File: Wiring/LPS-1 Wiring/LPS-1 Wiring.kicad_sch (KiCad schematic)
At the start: 25 parts, among them J1 Block_Connector_01_b, J10 Block_Connector_01_b, J101 Block_Connector_01_b, J102 Block_Connector_01_b, J11 Block_Connector_01_b, J12 Block_Connector_01_b, J2 Block_Connector_01_b, J3 Block_Connector_01_b, J4 Block_Connector_01_b, J5 Block_Connector_01_b, J500 GND Block, J6 Block_Connector_01_b, J7 Pwr Block, J8 Block_Connector_01_b, J9 Block_Connector_01_b, SW2 TRU Components NO

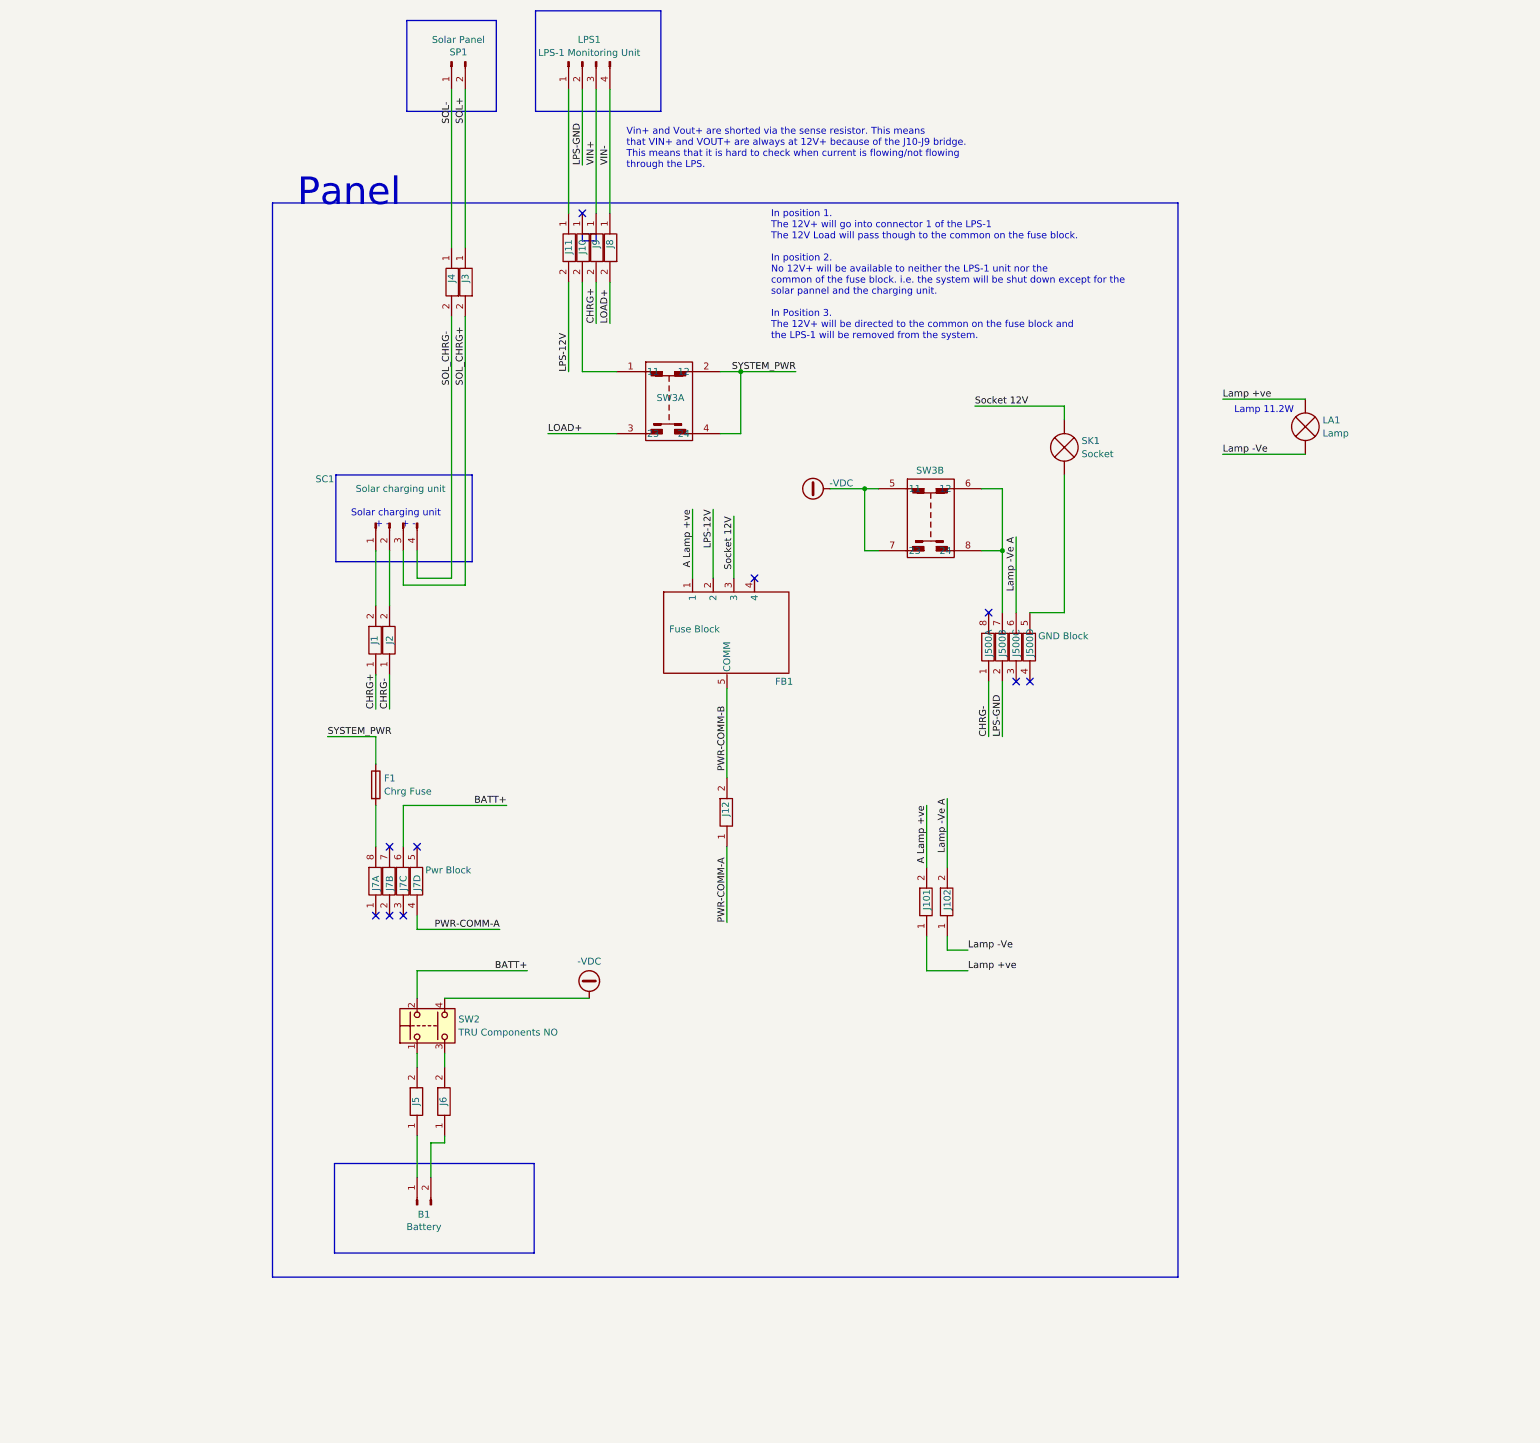
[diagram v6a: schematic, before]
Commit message: Reconfigured the LPS-1 wiring
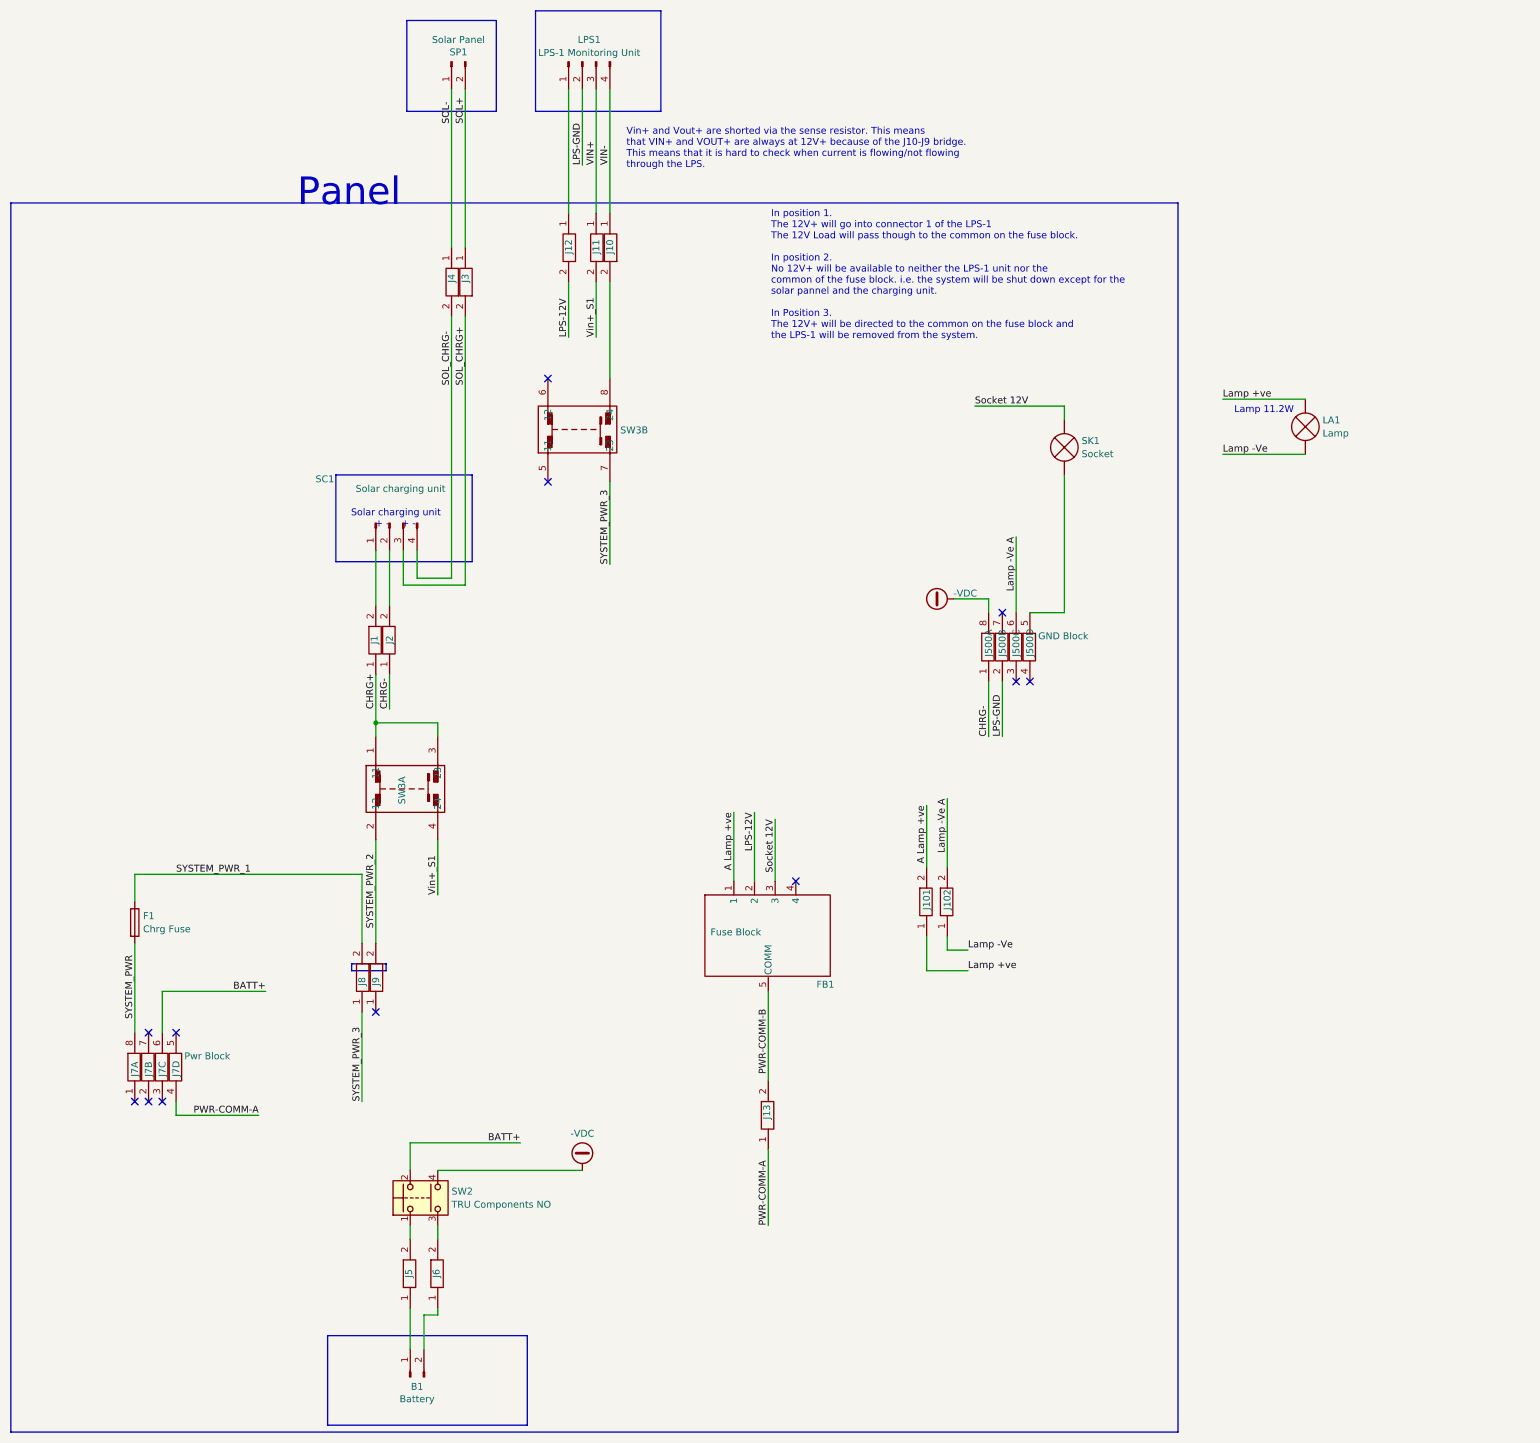
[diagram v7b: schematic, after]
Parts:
- removed J10: Block_Connector_01_b, Wiring:Degson_01_PC2.5-01P-11-00AH-1_5.2, symbol Wiring:Block_Connector_01_Pin
- added J8, J9: Block_Connector_01_b, Wiring:Degson_01_PC2.5-01P-11-00AH-1_5.2, symbol Wiring:Block_Connector_01_Pin
- renumbered J8 to J10, J9 to J11, J11 to J12, J12 to J13
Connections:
- net -VDC: now also J500.8; no longer SW3.5 (11), SW3.7 (23)
- net CHRG+: now also SW3.1 (11), SW3.3 (23); no longer J11.2
- net SYSTEM_PWR: now also F1.2, J7.8; no longer F1.1, SW3.2 (12), SW3.4 (24)
- net LOAD+: no longer names the net of J10.2
- net LOAD+: now also SW3.8 (24); no longer SW3.3 (23)
- new net SYSTEM_PWR_1: F1.1, J8.2
- new net SYSTEM_PWR_2: J9.2, SW3.2 (12)
- new net SYSTEM_PWR_3: J8.1, SW3.7 (23)
- new net Vin+_S1: J11.2, SW3.4 (24)
- now unconnected: J500.7, SW3.6 (12)
- no-connect marks 10 -> 12
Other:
- moved on the sheet: B1, F1, FB1, J13, J5, J6, J7A, J7B, J7C, J7D, SW2, SW3A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

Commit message: Panel wiring update
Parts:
- added J13: Block_Connector_01_b, Wiring:Degson_01_PC2.5-01P-11-00AH-1_5.2, symbol Wiring:Block_Connector_01_Pin
- renumbered J13 to J14
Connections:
- net LPS-12V: now also J12.1, LPS1.1 (Pin_1); no longer FB1.2, J12.2
- net LPS-12V_2: now reaches SW3.5 (11)
- net LPS-12V_2: now also J13.2
- net LPS-12V_3: now reaches SW3.6 (12)
- net LPS-12V_3: now also J12.2
- net VIN+ renamed Vin+
- net VIN- renamed Vout+
- new net LPS-12V_1: FB1.2, J13.1
- no-connect marks 12 -> 10
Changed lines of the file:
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@@
 	)
 	(no_connect
-		(at 146.05 83.82)
-	)
-	(no_connect
-		(at 146.05 102.87)
-	)
-	(no_connect
 		(at 74.93 217.17)
 	)
@@
 	(wire
 		(pts
+			(xy 149.86 76.2) (xy 146.05 76.2)
+		)
+		(stroke
+			(width 0)
+			(type default)
+		)
+	)
+	(wire
+		(pts
+			(xy 146.05 76.2) (xy 146.05 83.82)
+		)
+		(stroke
+			(width 0)
+			(type default)
+		)
+	)
+	(wire
+		(pts
 			(xy 125.73 229.87) (xy 152.4 229.87)
 		)
@@
 	(wire
 		(pts
+			(xy 146.05 125.73) (xy 146.05 135.89)
+		)
+		(stroke
+			(width 0)
+			(type default)
+		)
+	)
+	(wire
+		(pts
 			(xy 77.47 219.71) (xy 92.71 219.71)
 		)
@@
 	(wire
 		(pts
+			(xy 146.05 102.87) (xy 146.05 113.03)
+		)
+		(stroke
+			(width 0)
+			(type default)
+		)
+	)
+	(wire
+		(pts
 			(xy 224.79 88.9) (xy 241.3 88.9)
 		)
@@
 		)
 	)
-	(label "VIN+"
+	(label "Vin+"
 		(at 154.94 44.45 90)
 		(effects
@@
 		)
 	)
+	(label "LPS-12V_2"
+		(at 146.05 113.03 90)
+		(effects
+			(font
+				(size 1.27 1.27)
+			)
+			(justify left bottom)
+		)
+	)
 	(label "LPS-GND"
 		(at 229.87 149.86 90)
@@
 	)
 	(label "LPS-12V"
-		(at 184.15 163.83 270)
+		(at 149.86 44.45 90)
 		(effects
 			(font
 				(size 1.27 1.27)
 			)
-			(justify right bottom)
+			(justify left bottom)
 		)
 	)
@@
 		)
 	)
+	(label "LPS-12V_1"
+		(at 184.15 163.83 270)
+		(effects
+			(font
+				(size 1.27 1.27)
+			)
+			(justify right bottom)
+		)
+	)
 	(label "CHRG+"
 		(at 114.3 144.78 90)
@@
 		)
 	)
-	(label "LPS-12V"
-		(at 149.86 76.2 90)
+	(label "LPS-12V_1"
+		(at 146.05 135.89 90)
+		(effects
+			(font
+				(size 1.27 1.27)
+			)
+			(justify left bottom)
+		)
+	)
+	(label "LPS-12V_3"
+		(at 146.05 81.28 90)
 		(effects
 			(font
@@
 		)
 	)
-	(label "VIN-"
+	(label "Vout+"
 		(at 157.48 44.45 90)
 		(effects
@@
 		(in_pos_files yes)
 		(dnp no)
-		(property "Reference" "J13"
+		(property "Reference" "J14"
 			(at 186.436 220.472 90)
 			(show_name no)
@@
 			(project "LPS-1 Wiring"
 				(path "/b9731cf8-57f6-454f-95de-12f1db0e3ec9"
-					(reference "J13")
+					(reference "J14")
 					(unit 1)
 				)
@@
 				)
 			)
+		)
+	)
+	(symbol
+		(lib_id "Wiring:Block_Connector_01_Pin")
+		(at 146.05 119.38 0)
+		(unit 1)
+		(body_style 1)
+		(exclude_from_sim no)
+		(in_bom yes)
+		(on_board yes)
+		(in_pos_files yes)
+		(dnp no)
+		(property "Reference" "J13"
+			(at 145.796 120.142 90)
+			(show_name no)
+			(do_not_autoplace no)
+			(effects
+				(font
+					(size 1.27 1.27)
+				)
+				(justify left)
+			)
+		)
+		(property "Value" "Block_Connector_01_b"
+			(at 147.701 120.5921 0)
+			(hide yes)
+			(show_name no)
+			(do_not_autoplace no)
+			(effects
+				(font
+					(size 1.27 1.27)
+				)
+				(justify left)
+			)
+		)
+		(property "Footprint" "Wiring:Degson_01_PC2.5-01P-11-00AH-1_5.2"
+			(at 146.05 108.458 0)
+			(hide yes)
+			(show_name no)
+			(do_not_autoplace no)
+			(effects
+				(font
+					(size 1.27 1.27)
+				)
+			)
+		)
+		(property "Datasheet" ""
+			(at 146.05 119.38 0)
+			(hide yes)
+			(show_name no)
+			(do_not_autoplace no)
+			(effects
+				(font
+					(size 1.27 1.27)
+				)
+			)
+		)
+		(property "Description" "Generic Connector Block"
+			(at 146.05 110.744 0)
+			(hide yes)
+			(show_name no)
+			(do_not_autoplace no)
+			(effects
+				(font
+					(size 1.27 1.27)
+				)
+			)
+		)
+		(property "MPN" ""
+			(at 146.05 119.38 0)
+			(hide yes)
+			(show_name no)
+			(do_not_autoplace no)
+			(effects
+				(font
+					(size 1.27 1.27)
+				)
+			)
+		)
+		(property "Link" ""
+			(at 146.05 119.38 0)
+			(hide yes)
+			(show_name no)
+			(do_not_autoplace no)
+			(effects
+				(font
+					(size 1.27 1.27)
+				)
+			)
+		)
+		(property "Comp_Name" ""
+			(at 146.05 119.38 0)
+			(show_name no)
+			(do_not_autoplace no)
+			(effects
+				(font
+					(size 1.27 1.27)
+				)
+			)
+		)
+		(pin "1"
+		)
+		(pin "2"
+		)
+		(instances
+			(project "LPS-1 Wiring"
+				(path "/b9731cf8-57f6-454f-95de-12f1db0e3ec9"
+					(reference "J13")
+					(unit 1)
+				)
+			)
